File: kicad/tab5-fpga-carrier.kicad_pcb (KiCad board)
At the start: 4 copper layers, 125 x 78 mm, 100 parts, among them J1 DC 12-24V, J2 USB-C PD in, J3 M5-BUS (to Tab5), J4 Tang Primer 20K Core, J5 HDMI OUT, J6 PMOD1, J7 PMOD2, J8 GPIO pads, Q1 2N7002, Q2 2N7002, SW1 SW, SW2 RESET (Tab5), SW3 FPGA ON/OFF, U1 CH224K, U2 TPS5430DDAR, U3 AMS1117-3.3, U4 RCLAMP0524P, U5 RCLAMP0524P, U6 SRV05-4

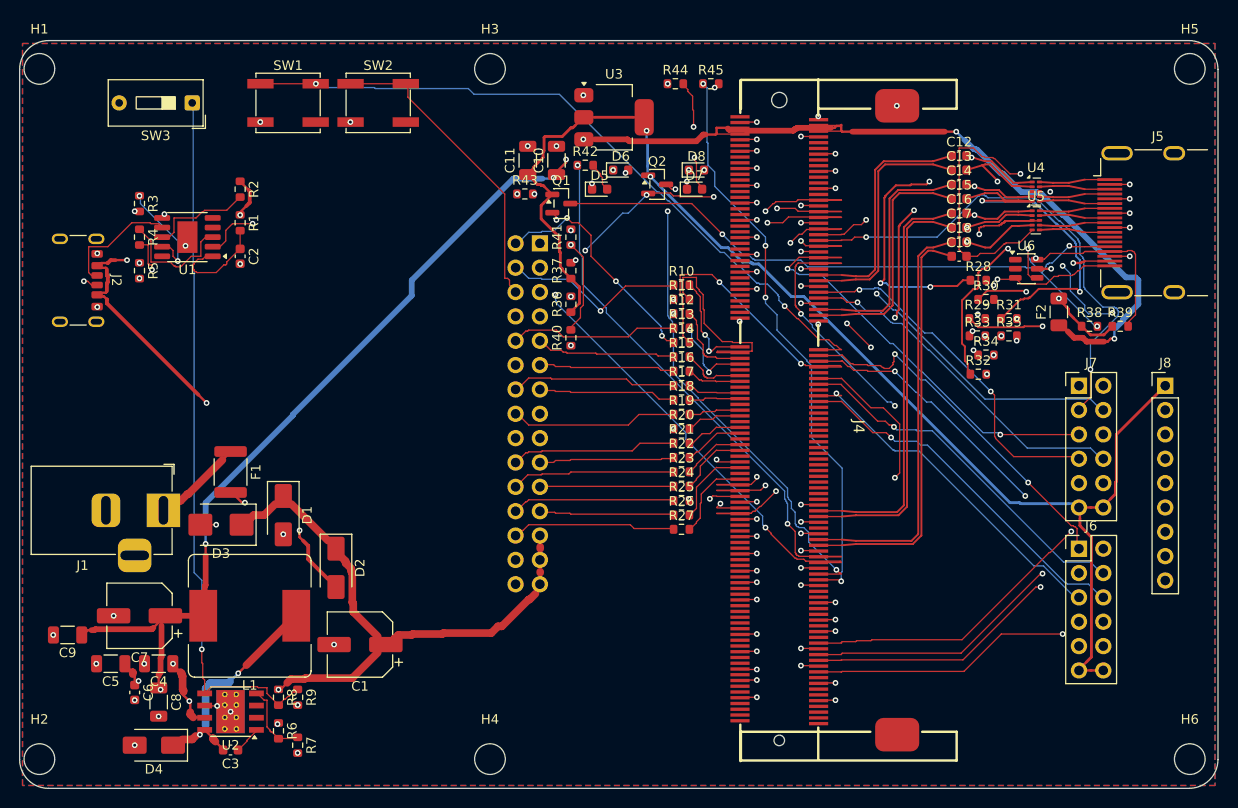
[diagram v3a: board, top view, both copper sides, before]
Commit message: HDMI remediation after independent audit: copper-continuous ESD, short 499R branches, re-routed pairs, re-simulated channel
- ESD (RClamp0524P, C293965): I/O pins joined to the TMDS line by copper straps, no reliance on part-internal pass-through
- 499 ohm bias resistors moved next to the tap (branches 2-11.5 mm), routed and modelled as terminated lines
- route_pcb: roles JSON (main/branch), pair routing, 113/113 nets, DRC 0/0
- sim: ordered-segment extraction without silent fallback, branch/ESD channel model, continuity check, variants
- report page, docs (section 10), README, BOM updated; open items disclosed (D1N branch 11.5 mm, 3D uncalibrated)

Co-Authored-By: Claude Sonnet 5.5 <noreply@anthropic.com>
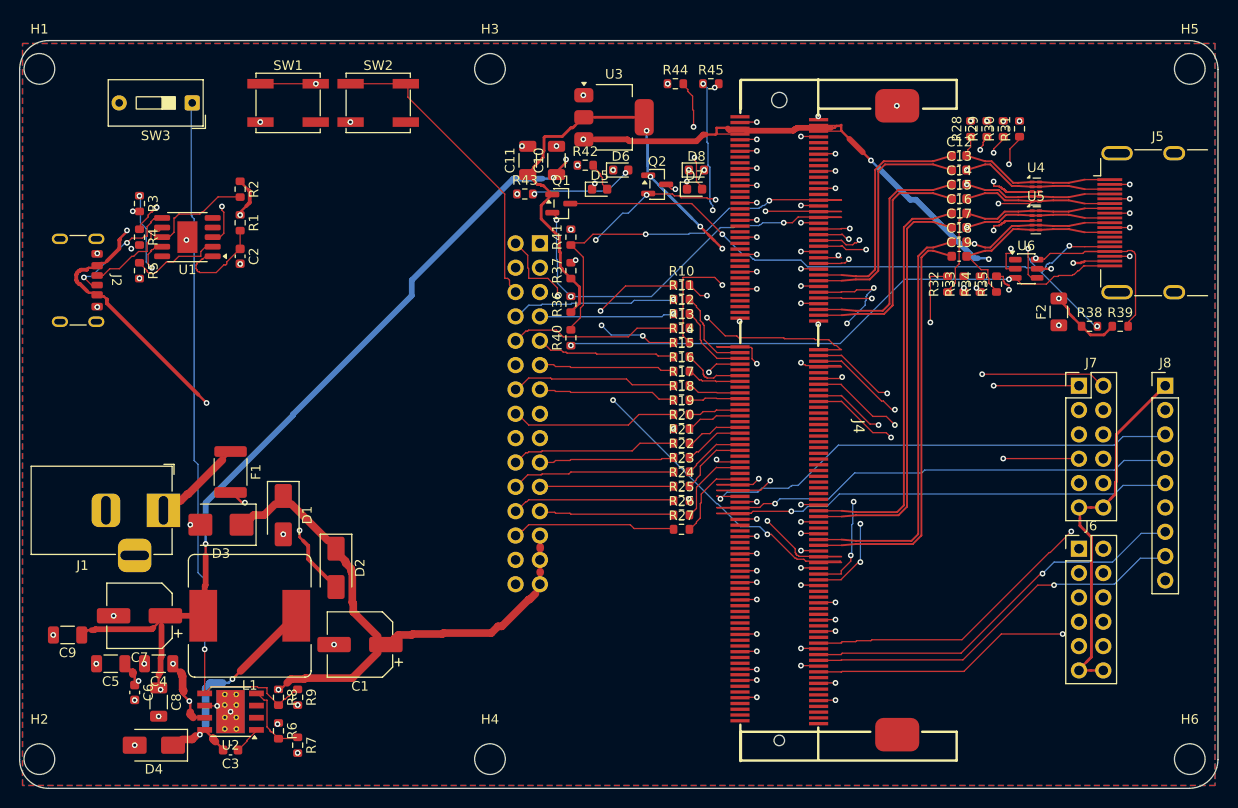
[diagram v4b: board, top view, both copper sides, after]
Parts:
- moved R31 19.8 mm to (106.3, 10.2), turned to 90 degrees
- moved R29 19.8 mm to (102.9, 10.2), turned to 90 degrees
- moved R30 17.9 mm to (104.6, 10.2), turned to 90 degrees
- moved R28 15.8 mm to (101.2, 10.2), turned to 90 degrees
- moved R32 9.93 mm to (98.8, 26.4), turned to 90 degrees
- moved R34 7.42 mm to (102.2, 26.4), turned to 90 degrees
- moved R33 5.58 mm to (100.5, 26.4), turned to 90 degrees
- moved R35 5.55 mm to (103.9, 26.4), turned to 90 degrees
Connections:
- J5 pad 1: HDMI_D2P_K -> HDMI_D2P_C
- J5 pad 10: HDMI_CKP_K -> HDMI_CKP_C
- J5 pad 12: HDMI_CKN_K -> HDMI_CKN_C
- J5 pad 3: HDMI_D2N_K -> HDMI_D2N_C
- J5 pad 4: HDMI_D1P_K -> HDMI_D1P_C
- J5 pad 6: HDMI_D1N_K -> HDMI_D1N_C
- J5 pad 7: HDMI_D0P_K -> HDMI_D0P_C
- J5 pad 9: HDMI_D0N_K -> HDMI_D0N_C
- U4 pad 10: HDMI_D2P_K -> HDMI_D2P_C
- U4 pad 6: HDMI_D1N_K -> HDMI_D1N_C
- U4 pad 7: HDMI_D1P_K -> HDMI_D1P_C
- U4 pad 9: HDMI_D2N_K -> HDMI_D2N_C
- U5 pad 10: HDMI_D0P_K -> HDMI_D0P_C
- U5 pad 6: HDMI_CKN_K -> HDMI_CKN_C
- U5 pad 7: HDMI_CKP_K -> HDMI_CKP_C
- U5 pad 9: HDMI_D0N_K -> HDMI_D0N_C
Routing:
- net HDMI_CKN_C: track 61.4 -> 21.3 mm, vias 2 -> 0
- net HDMI_D2N_C: track 40.2 -> 20.4 mm
- net +5V: track 194.2 -> 174.7 mm, vias 8 -> 9
- net HDMI_D2P_C: track 37.7 -> 18.2 mm, vias 4 -> 0
- net P2_1: track 53.0 -> 35.6 mm, vias 2 -> 1
- net HDMI_CKP_C: track 37.1 -> 21.2 mm, vias 4 -> 2
- net GND: track 119.6 -> 134.8 mm
- net F_RDY: track 22.0 -> 9.06 mm
- net HDMI_D1N_C: track 39.0 -> 26.9 mm
- net P2_6: track 49.4 -> 37.4 mm, vias 2 -> 1
- net P2_2: track 46.1 -> 35.7 mm, vias 2 -> 1
- net PD_CFG2: track 19.3 -> 9.57 mm, vias 2 -> 0
- net P2_5: track 45.6 -> 36.8 mm, vias 2 -> 1
- net F_AUX0: track 11.1 -> 19.5 mm
- net HDMI_D0N_C: track 30.5 -> 22.2 mm
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
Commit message: HDMI second-audit remediation (A1-A5): ESD footprint, escape stubs, 4-port P/N model, combined sensitivity, checks, report r3
- A1: dedicated DFN2510-10L_RCLAMP0524P footprint (GND land 0.30->0.42 mm), symbol IO/NC, datasheet comparison + check_esd_footprint.py
- A2: router roles stub/strap, check_classification.py (0 unclassified), pad-clipped escape stubs added to the analysed path
- A3: 4-port P/N ABCD channel model, P/N branches at their own taps, SCD21; short-symmetric-branch comparison
- A4: Core Z x ESD C matrix; fails -10 dB at Core 85 ohm with ESD >= 0.35 pF (D1)
- A5: check_continuity pin-number check + exit codes, check_negative.py, manifest_r3.json, D2 inversion doc, README/site updated
- New report site/hdmi-simulation-r3.html (r1/r2 kept); re-routed 113/113 nets, DRC 0/0
- Not done: 3D calibration (B), MeOS requirements (C)

Co-Authored-By: Claude Sonnet 5.5 <noreply@anthropic.com>
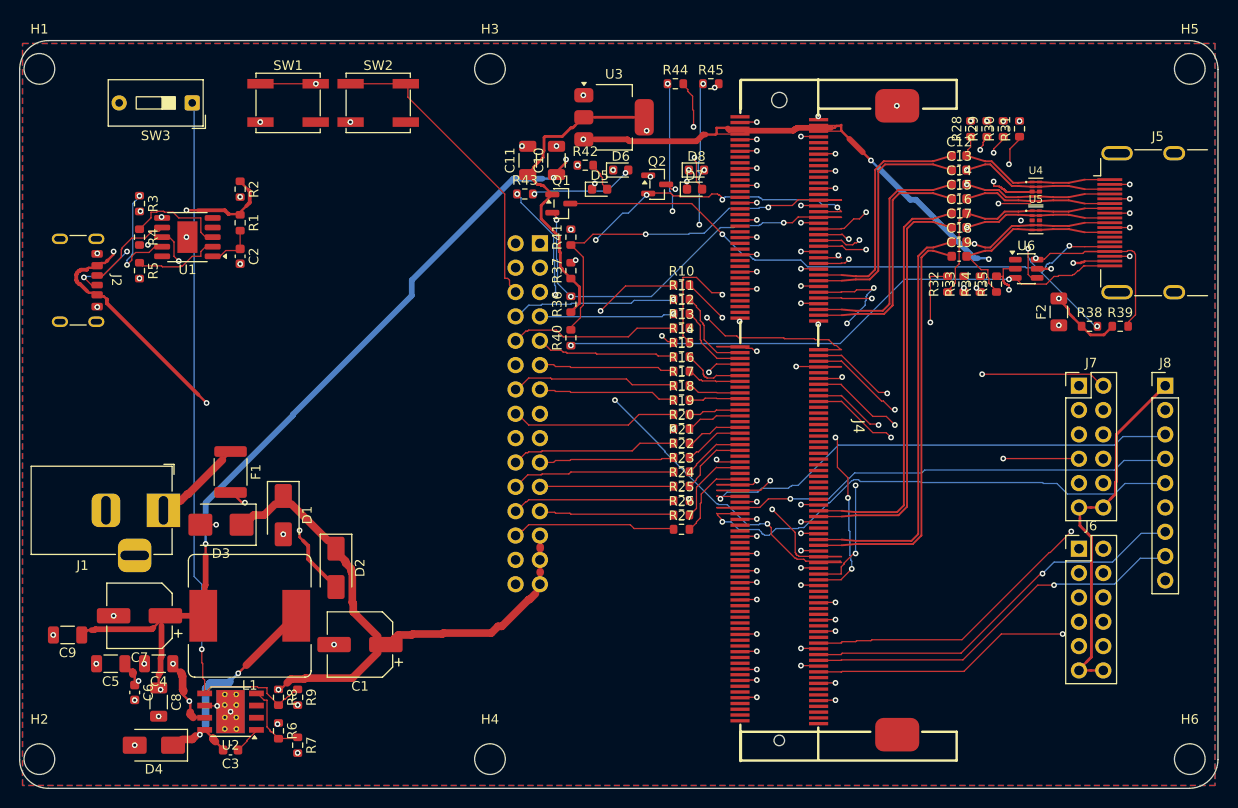
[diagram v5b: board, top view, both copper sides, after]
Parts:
- U4, U5: footprint USON-10_2.5x1.0mm_P0.5mm -> DFN2510-10L_RCLAMP0524P
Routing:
- net GND: track 134.8 -> 124.3 mm, vias 94 -> 93
- net PD_VDD: track 10.4 -> 5.13 mm
- net PD_CFG3: track 14.2 -> 10.7 mm, vias 2 -> 0
- net GPIO2: track 50.5 -> 53.9 mm
- net F_AUX0: track 19.5 -> 16.7 mm
- net PD_VBUS_S: track 10.7 -> 13.0 mm, vias 0 -> 2
- net M_CLK: track 22.7 -> 20.8 mm, vias 3 -> 1
- net P2_0: track 39.5 -> 41.2 mm, vias 2 -> 1
- net VIN: track 89.6 -> 88.2 mm
- net PD_CFG1: track 11.5 -> 12.5 mm
- net P1_3: track 46.6 -> 47.3 mm
- net PD_CFG2: track 9.57 -> 8.93 mm
- net F_HSDA: track 34.4 -> 35.0 mm
- net CC2: track 13.1 -> 12.6 mm, vias 2 -> 3
- net F_LED1: track 58.8 -> 59.3 mm, vias 3 -> 4
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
